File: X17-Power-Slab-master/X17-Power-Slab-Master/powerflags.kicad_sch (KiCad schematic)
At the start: 0 parts

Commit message: Schematic Updates
#SlayedTheDayAway
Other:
- note added: "General Labels"
- note added: "Power flags with same name are same all around even if it is input or output."

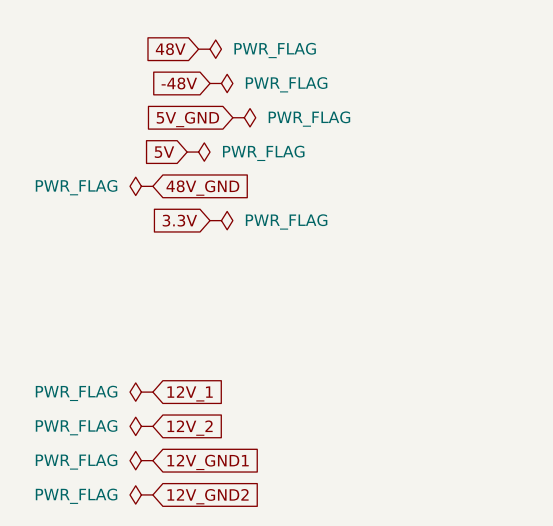
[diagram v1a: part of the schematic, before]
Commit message: Schematic Full Update
Probs can start pacing after this.
Diode on RVP changed,
Button changed
Reverse voltage updated
Symbols updated to remove DRCs
GNDs changed
Connector updated
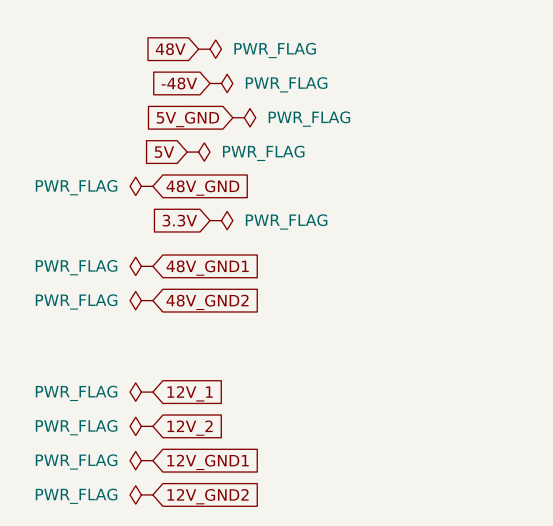
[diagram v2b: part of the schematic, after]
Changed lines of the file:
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@@
+		)
+	)
+	(global_label "48V_GND1"
+		(shape input)
+		(at 36.83 82.55 0)
+		(fields_autoplaced yes)
+		(effects
+			(font
+				(size 1.27 1.27)
+			)
+			(justify left)
+		)
+		(property "Intersheetrefs" "${INTERSHEET_REFS}"
+			(at 49.3704 82.55 0)
+			(effects
+				(font
+					(size 1.27 1.27)
+				)
+				(justify left)
+				(hide yes)
+			)
+		)
+	)
+	(global_label "48V_GND2"
+		(shape input)
+		(at 36.83 86.36 0)
+		(fields_autoplaced yes)
+		(effects
+			(font
+				(size 1.27 1.27)
+			)
+			(justify left)
+		)
+		(property "Intersheetrefs" "${INTERSHEET_REFS}"
+			(at 49.3704 86.36 0)
+			(effects
+				(font
+					(size 1.27 1.27)
+				)
+				(justify left)
+				(hide yes)
+			)
 		)
 	)
@@
 	(symbol
 		(lib_id "power:PWR_FLAG")
+		(at 36.83 86.36 90)
+		(unit 1)
+		(exclude_from_sim no)
+		(in_bom yes)
+		(on_board yes)
+		(dnp no)
+		(fields_autoplaced yes)
+		(property "Reference" "#FLG012"
+			(at 34.925 86.36 0)
+			(effects
+				(font
+					(size 1.27 1.27)
+				)
+				(hide yes)
+			)
+		)
+		(property "Value" "PWR_FLAG"
+			(at 33.02 86.3599 90)
+			(effects
+				(font
+					(size 1.27 1.27)
+				)
+				(justify left)
+			)
+		)
+		(property "Footprint" ""
+			(at 36.83 86.36 0)
+			(effects
+				(font
+					(size 1.27 1.27)
+				)
+				(hide yes)
+			)
+		)
+		(property "Datasheet" "~"
+			(at 36.83 86.36 0)
+			(effects
+				(font
+					(size 1.27 1.27)
+				)
+				(hide yes)
+			)
+		)
+		(property "Description" "Special symbol for telling ERC where power comes from"
+			(at 36.83 86.36 0)
+			(effects
+				(font
+					(size 1.27 1.27)
+				)
+				(hide yes)
+			)
+		)
+		(pin "1"
+		)
+		(instances
+			(project "X17-Power-Slab-Master"
+				(path "/57e59c68-7be1-495e-b535-e78e0f561e15/42b101a3-9efa-41cd-8318-19548b11d7e8"
+					(reference "#FLG012")
+					(unit 1)
+				)
+			)
+		)
+	)
+	(symbol
+		(lib_id "power:PWR_FLAG")
 		(at 36.83 100.33 90)
 		(unit 1)
@@
 					(unit 1)
 				)
+			)
+		)
+	)
+	(symbol
+		(lib_id "power:PWR_FLAG")
+		(at 36.83 82.55 90)
+		(unit 1)
+		(exclude_from_sim no)
+		(in_bom yes)
+		(on_board yes)
+		(dnp no)
+		(fields_autoplaced yes)
+		(property "Reference" "#FLG011"
+			(at 34.925 82.55 0)
+			(effects
+				(font
+					(size 1.27 1.27)
+				)
+				(hide yes)
+			)
+		)
+		(property "Value" "PWR_FLAG"
+			(at 33.02 82.5499 90)
+			(effects
+				(font
+					(size 1.27 1.27)
+				)
+				(justify left)
+			)
+		)
+		(property "Footprint" ""
+			(at 36.83 82.55 0)
+			(effects
+				(font
+					(size 1.27 1.27)
+				)
+				(hide yes)
+			)
+		)
+		(property "Datasheet" "~"
+			(at 36.83 82.55 0)
+			(effects
+				(font
+					(size 1.27 1.27)
+				)
+				(hide yes)
+			)
+		)
+		(property "Description" "Special symbol for telling ERC where power comes from"
+			(at 36.83 82.55 0)
+			(effects
+				(font
+					(size 1.27 1.27)
+				)
+				(hide yes)
+			)
+		)
+		(pin "1"
+		)
+		(instances
+			(project "X17-Power-Slab-Master"
+				(path "/57e59c68-7be1-495e-b535-e78e0f561e15/42b101a3-9efa-41cd-8318-19548b11d7e8"
+					(reference "#FLG011")
+					(unit 1)
+				)

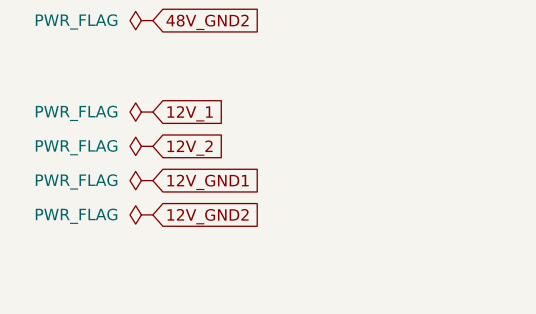
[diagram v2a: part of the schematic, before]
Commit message: Initial Placements
Issue - NRST_PSB is apparently ground flag
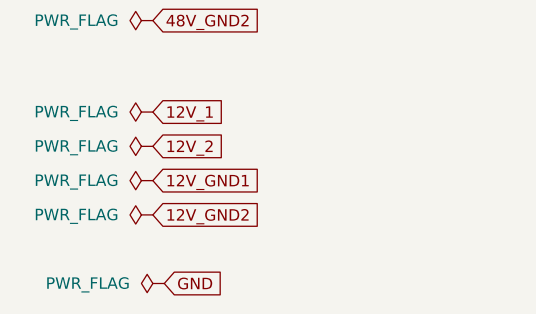
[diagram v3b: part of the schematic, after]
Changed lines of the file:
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@@
+		)
+	)
+	(global_label "GND"
+		(shape input)
+		(at 38.1 115.57 0)
+		(fields_autoplaced yes)
+		(effects
+			(font
+				(size 1.27 1.27)
+			)
+			(justify left)
+		)
+		(property "Intersheetrefs" "${INTERSHEET_REFS}"
+			(at 44.9557 115.57 0)
+			(effects
+				(font
+					(size 1.27 1.27)
+				)
+				(justify left)
+				(hide yes)
+			)
 		)
 	)
@@
 					(unit 1)
 				)
+			)
+		)
+	)
+	(symbol
+		(lib_id "power:PWR_FLAG")
+		(at 38.1 115.57 90)
+		(unit 1)
+		(exclude_from_sim no)
+		(in_bom yes)
+		(on_board yes)
+		(dnp no)
+		(fields_autoplaced yes)
+		(property "Reference" "#FLG013"
+			(at 36.195 115.57 0)
+			(effects
+				(font
+					(size 1.27 1.27)
+				)
+				(hide yes)
+			)
+		)
+		(property "Value" "PWR_FLAG"
+			(at 34.29 115.5699 90)
+			(effects
+				(font
+					(size 1.27 1.27)
+				)
+				(justify left)
+			)
+		)
+		(property "Footprint" ""
+			(at 38.1 115.57 0)
+			(effects
+				(font
+					(size 1.27 1.27)
+				)
+				(hide yes)
+			)
+		)
+		(property "Datasheet" "~"
+			(at 38.1 115.57 0)
+			(effects
+				(font
+					(size 1.27 1.27)
+				)
+				(hide yes)
+			)
+		)
+		(property "Description" "Special symbol for telling ERC where power comes from"
+			(at 38.1 115.57 0)
+			(effects
+				(font
+					(size 1.27 1.27)
+				)
+				(hide yes)
+			)
+		)
+		(pin "1"
+		)
+		(instances
+			(project ""
+				(path "/57e59c68-7be1-495e-b535-e78e0f561e15/42b101a3-9efa-41cd-8318-19548b11d7e8"
+					(reference "#FLG013")
+					(unit 1)
+				)

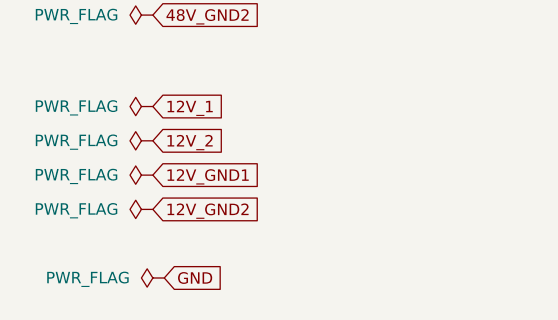
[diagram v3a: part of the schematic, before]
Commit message: Final First(?) Draft
NRST is stuck to general ground for whatever reason.

Test points wont connect for the life of me, will look @ in morning, will have sample plan.

Idea is there, really want to plan it out better 2nd time around. Alumni will give good tips!
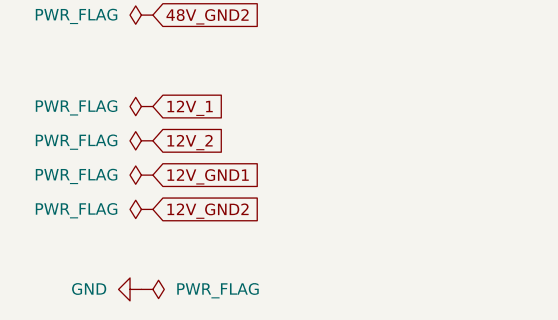
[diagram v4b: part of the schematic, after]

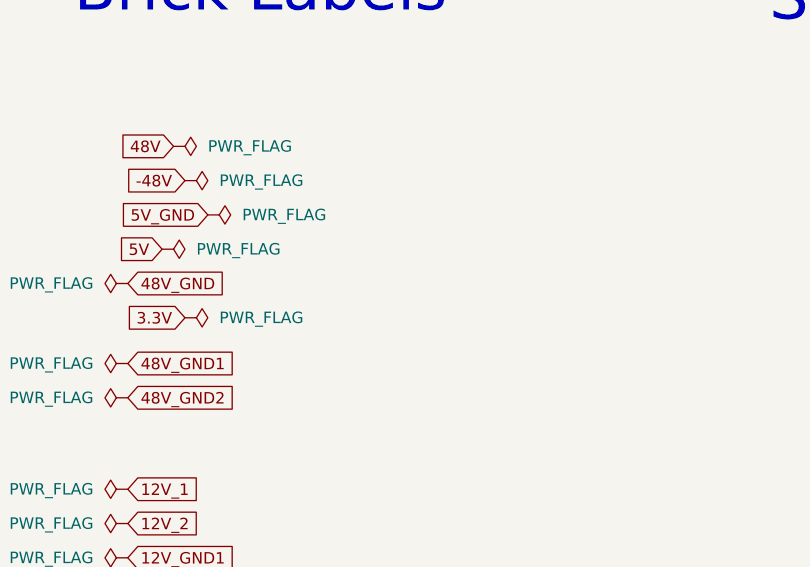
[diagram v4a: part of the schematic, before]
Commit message: Change to combined 12V 5V gnd
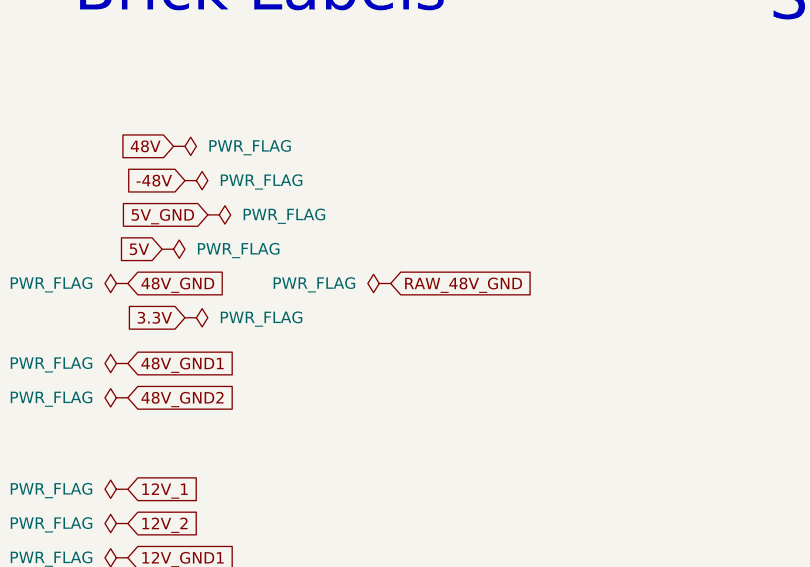
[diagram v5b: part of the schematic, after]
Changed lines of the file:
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@@
+		)
+	)
+	(global_label "RAW_48V_GND"
+		(shape input)
+		(at 66.04 73.66 0)
+		(fields_autoplaced yes)
+		(effects
+			(font
+				(size 1.27 1.27)
+			)
+			(justify left)
+		)
+		(property "Intersheetrefs" "${INTERSHEET_REFS}"
+			(at 82.1485 73.66 0)
+			(effects
+				(font
+					(size 1.27 1.27)
+				)
+				(justify left)
+				(hide yes)
+			)
 		)
 	)
@@
 					(unit 1)
 				)
+			)
+		)
+	)
+	(symbol
+		(lib_id "power:PWR_FLAG")
+		(at 66.04 73.66 90)
+		(unit 1)
+		(exclude_from_sim no)
+		(in_bom yes)
+		(on_board yes)
+		(dnp no)
+		(fields_autoplaced yes)
+		(property "Reference" "#FLG014"
+			(at 64.135 73.66 0)
+			(effects
+				(font
+					(size 1.27 1.27)
+				)
+				(hide yes)
+			)
+		)
+		(property "Value" "PWR_FLAG"
+			(at 62.23 73.6599 90)
+			(effects
+				(font
+					(size 1.27 1.27)
+				)
+				(justify left)
+			)
+		)
+		(property "Footprint" ""
+			(at 66.04 73.66 0)
+			(effects
+				(font
+					(size 1.27 1.27)
+				)
+				(hide yes)
+			)
+		)
+		(property "Datasheet" "~"
+			(at 66.04 73.66 0)
+			(effects
+				(font
+					(size 1.27 1.27)
+				)
+				(hide yes)
+			)
+		)
+		(property "Description" "Special symbol for telling ERC where power comes from"
+			(at 66.04 73.66 0)
+			(effects
+				(font
+					(size 1.27 1.27)
+				)
+				(hide yes)
+			)
+		)
+		(pin "1"
+		)
+		(instances
+			(project "X17-Power-Slab-Master"
+				(path "/57e59c68-7be1-495e-b535-e78e0f561e15/42b101a3-9efa-41cd-8318-19548b11d7e8"
+					(reference "#FLG014")
+					(unit 1)
+				)

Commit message: final for 12/30 meeting
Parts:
- added D2: 48V, Red LED:WL-SMCW_0805, symbol Red LED:WL-SMCW_0805
- added D3: 12V, Red LED:WL-SMCW_0805, symbol Red LED:WL-SMCW_0805
- added D4: 5V, Red LED:WL-SMCW_0805, symbol Red LED:WL-SMCW_0805
- added D5: D_TVS, Diode_SMD:D_SMB_Handsoldering, symbol Device:D_TVS
- added R2: 3k, Resistor_SMD:R_0603_1608Metric_Pad0.98x0.95mm_HandSolder, symbol Device:R_US
- added R3: 250, Resistor_SMD:R_0603_1608Metric_Pad0.98x0.95mm_HandSolder, symbol Device:R_US
- added R4: 150, Resistor_SMD:R_0603_1608Metric_Pad0.98x0.95mm_HandSolder, symbol Device:R_US
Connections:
- net 48V: now also R2.1
- net 48V_GND: now also D2.1
- net 5V: now also R4.1
- new net: D4.2, R4.2
- new net: D2.2, R2.2
- new net: D3.2, R3.2
- new net 12V: D5.1 (A1), R3.1
- new net 12V_5V_GND: D3.1, D4.1, D5.2 (A2)
